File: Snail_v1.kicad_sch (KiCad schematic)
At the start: 2 parts, among them U1 PAM8406D, U2 STM32G431K6Tx

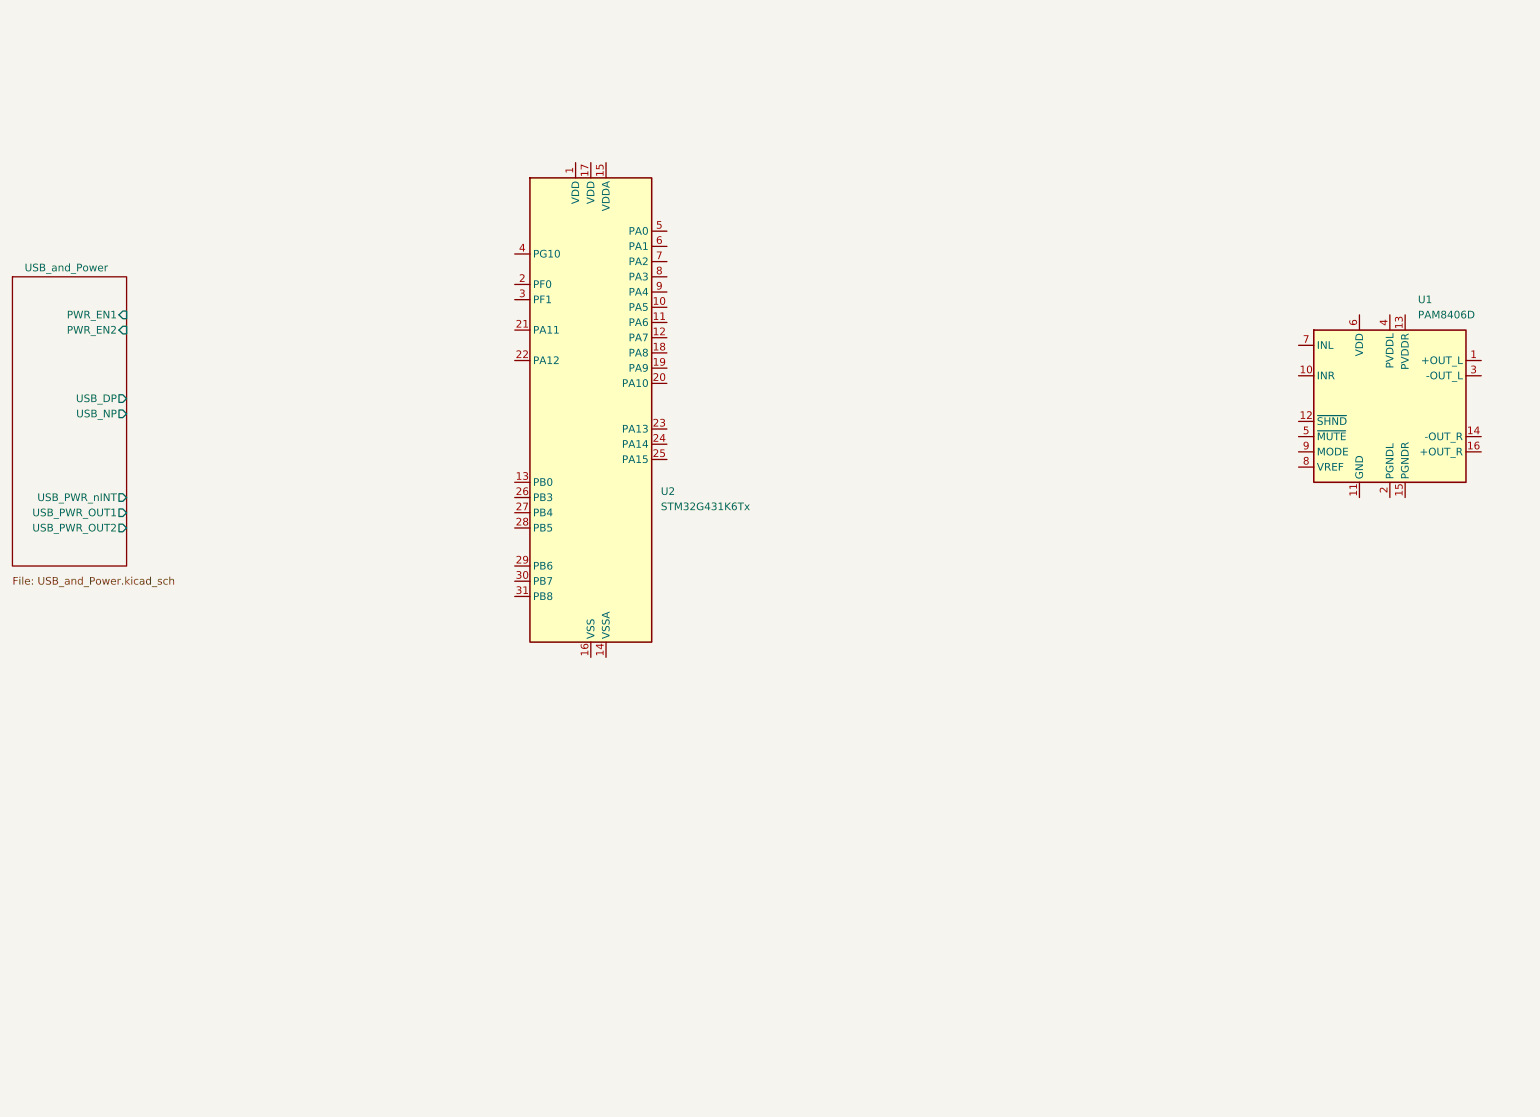
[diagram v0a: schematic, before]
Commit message: Added 5V, 3V3, PAM circuit
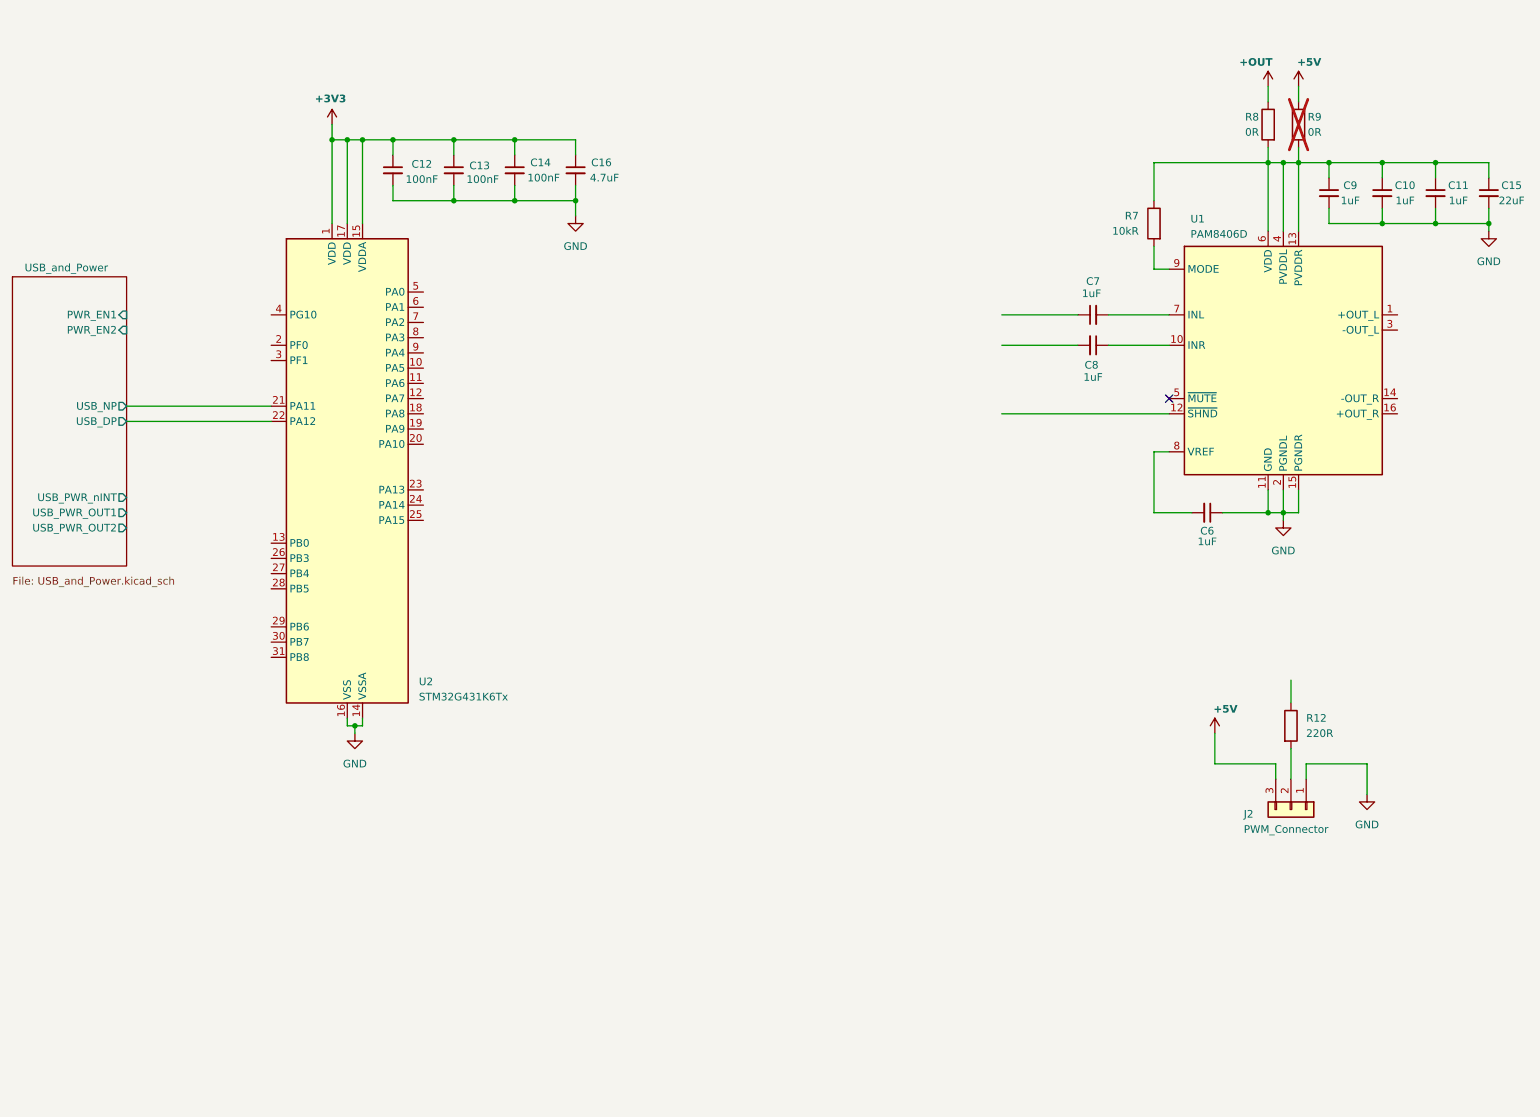
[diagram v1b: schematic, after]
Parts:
- added C10, C11, C6, C7, C8, C9: 1uF, symbol Device:C_Small
- added C12, C13, C14: 100nF, symbol Device:C_Small
- added C15: 22uF, symbol Device:C_Small
- added C16: 4.7uF, symbol Device:C_Small
- added J2: PWM_Connector, symbol Connector_Generic:Conn_01x03
- added R12: 220R, symbol Device:R
- added R7: 10kR, symbol Device:R
- added R8, R9: 0R, symbol Device:R
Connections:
- net USB_and_Power/USB_DP: now also U2.22 (PA12)
- net USB_and_Power/USB_NP: now also U2.21 (PA11)
- net at U1.10 (INR): now also C8.1
- net GND: now reaches U1.11 (GND)
- net GND: now also U1.15 (PGNDR), U1.2 (PGNDL), U2.14 (VSSA), U2.16 (VSS), U2.32 (VSS), C10.2, C11.2, C12.2, C13.2, C14.2, C15.2, C16.2, C6.1, C9.2, J2.1 (Pin_1)
- net at U1.13 (PVDDR): now also U1.4 (PVDDL), U1.6 (VDD), C10.1, C11.1, C15.1, C9.1, R7.1, R8.2, R9.2
- net at U1.7 (INL): now also C7.2
- net at U1.8 (VREF): now also C6.2
- net at U1.9 (MODE): now also R7.2
- net +3V3: now reaches U2.1 (VDD)
- net +3V3: now also U2.15 (VDDA), U2.17 (VDD), C12.1, C13.1, C14.1, C16.1
- new net: J2.2 (Pin_2), R12.2
- new net +5V: J2.3 (Pin_3), R9.1
- new net +OUT: R8.1
- no-connect marks 0 -> 1
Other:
- company: (none) -> Author: Christian R
- title: (none) -> Snail v1
- moved on the sheet: U1, U2

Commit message: Added BY25Q32 extFlash
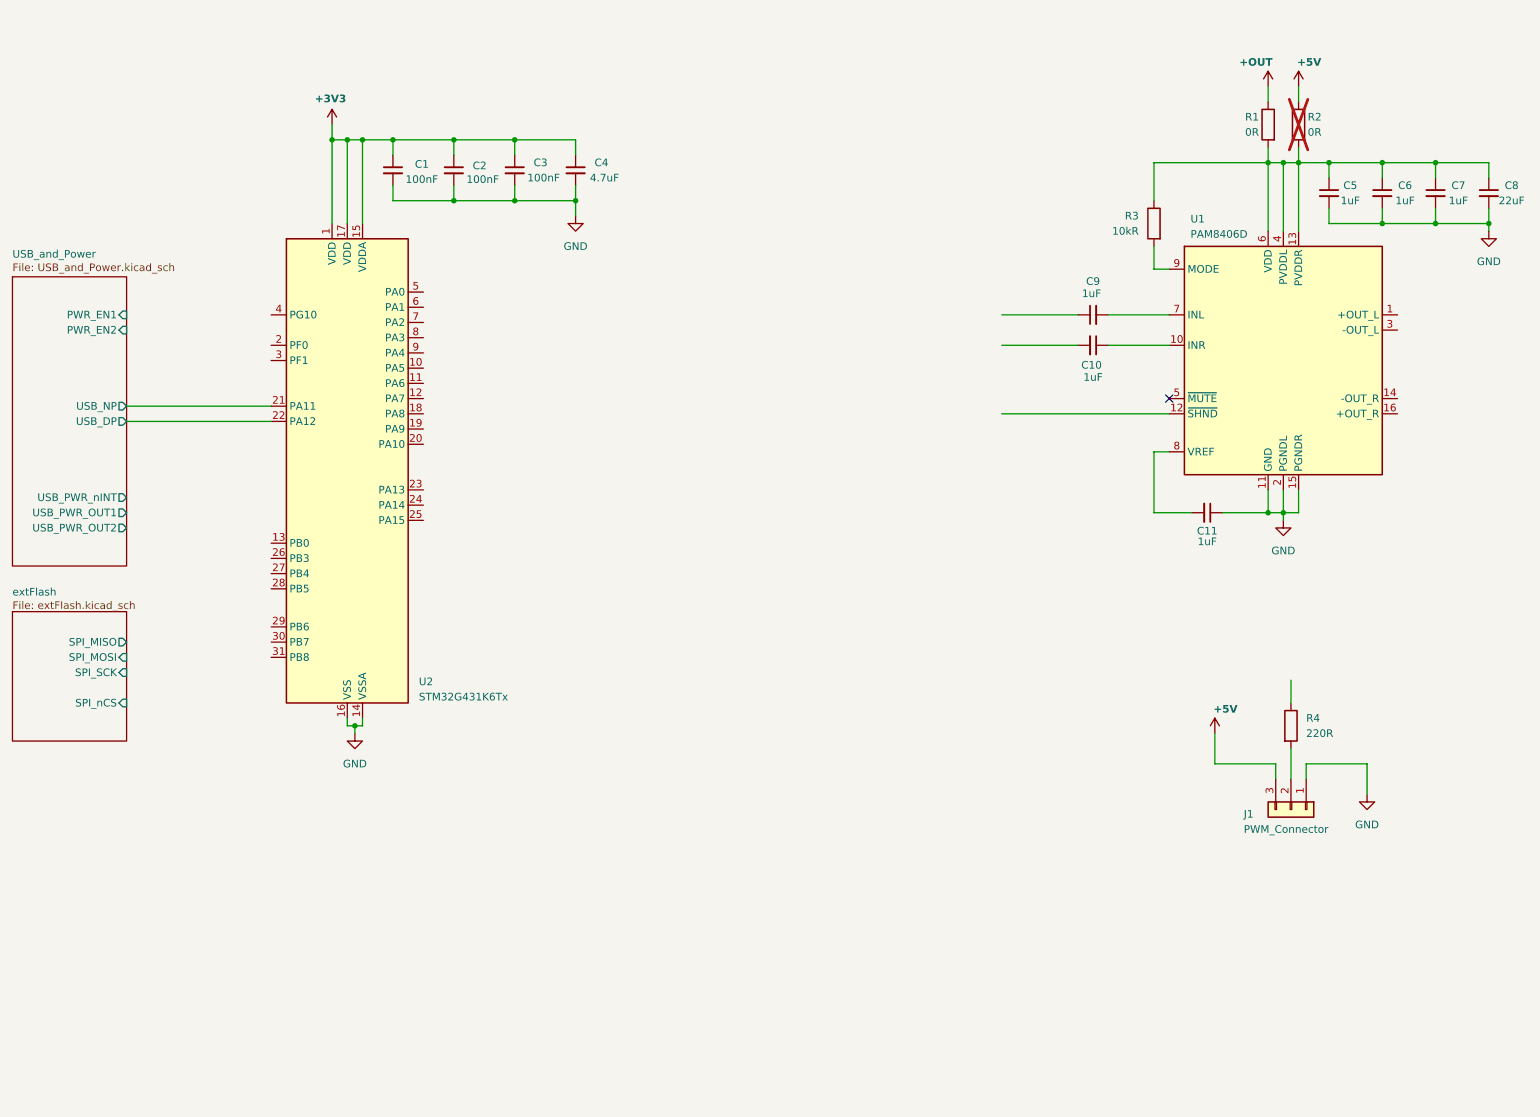
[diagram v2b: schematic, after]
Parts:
- renumbered C12 to C1, C8 to C10, C6 to C11, C13 to C2, C14 to C3, C16 to C4, C9 to C5, C10 to C6, C11 to C7, C15 to C8, C7 to C9, J2 to J1, R8 to R1, R9 to R2, R7 to R3, R12 to R4
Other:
- added sheet extFlash (extFlash.kicad_sch)
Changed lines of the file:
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@@
 		(on_board yes)
 		(dnp no)
-		(property "Reference" "#PWR023"
+		(property "Reference" "#PWR03"
 			(at 80.01 34.29 0)
 			(effects
@@
 			(project ""
 				(path "/98695d9f-8521-4f7d-bb41-f22c1215a8e7"
-					(reference "#PWR023")
+					(reference "#PWR03")
 					(unit 1)
 				)
@@
 		(dnp no)
 		(fields_autoplaced yes)
-		(property "Reference" "R12"
+		(property "Reference" "R4"
 			(at 242.57 129.5399 0)
 			(effects
@@
 			(project ""
 				(path "/98695d9f-8521-4f7d-bb41-f22c1215a8e7"
-					(reference "R12")
+					(reference "R4")
 					(unit 1)
 				)
@@
 		(on_board yes)
 		(dnp no)
-		(property "Reference" "C6"
+		(property "Reference" "C11"
 			(at 226.06 98.298 90)
 			(effects
@@
 			(project ""
 				(path "/98695d9f-8521-4f7d-bb41-f22c1215a8e7"
-					(reference "C6")
+					(reference "C11")
 					(unit 1)
 				)
@@
 		(dnp no)
 		(fields_autoplaced yes)
-		(property "Reference" "#PWR014"
+		(property "Reference" "#PWR06"
 			(at 238.76 102.87 0)
 			(effects
@@
 			(project ""
 				(path "/98695d9f-8521-4f7d-bb41-f22c1215a8e7"
-					(reference "#PWR014")
+					(reference "#PWR06")
 					(unit 1)
 				)
@@
 		(on_board yes)
 		(dnp no)
-		(property "Reference" "#PWR025"
+		(property "Reference" "#PWR08"
 			(at 227.33 135.89 0)
 			(effects
@@
 			(project "Snail_v1"
 				(path "/98695d9f-8521-4f7d-bb41-f22c1215a8e7"
-					(reference "#PWR025")
+					(reference "#PWR08")
 					(unit 1)
 				)
@@
 		(on_board yes)
 		(dnp no)
-		(property "Reference" "C16"
+		(property "Reference" "C4"
 			(at 124.968 36.83 0)
 			(effects
@@
 			(project "Snail_v1"
 				(path "/98695d9f-8521-4f7d-bb41-f22c1215a8e7"
-					(reference "C16")
+					(reference "C4")
 					(unit 1)
 				)
@@
 		(dnp no)
 		(fields_autoplaced yes)
-		(property "Reference" "#PWR013"
+		(property "Reference" "#PWR07"
 			(at 83.82 138.43 0)
 			(effects
@@
 			(project ""
 				(path "/98695d9f-8521-4f7d-bb41-f22c1215a8e7"
-					(reference "#PWR013")
+					(reference "#PWR07")
 					(unit 1)
 				)
@@
 		(on_board yes)
 		(dnp no)
-		(property "Reference" "R7"
+		(property "Reference" "R3"
 			(at 214.63 45.7199 0)
 			(effects
@@
 			(project ""
 				(path "/98695d9f-8521-4f7d-bb41-f22c1215a8e7"
-					(reference "R7")
+					(reference "R3")
 					(unit 1)
 				)
@@
 		(on_board yes)
 		(dnp no)
-		(property "Reference" "C9"
+		(property "Reference" "C5"
 			(at 249.936 40.64 0)
 			(effects
@@
 			(project "Snail_v1"
 				(path "/98695d9f-8521-4f7d-bb41-f22c1215a8e7"
-					(reference "C9")
+					(reference "C5")
 					(unit 1)
 				)
@@
 		(on_board yes)
 		(dnp no)
-		(property "Reference" "C15"
+		(property "Reference" "C8"
 			(at 276.86 40.64 0)
 			(effects
@@
 			(project "Snail_v1"
 				(path "/98695d9f-8521-4f7d-bb41-f22c1215a8e7"
-					(reference "C15")
+					(reference "C8")
 					(unit 1)
 				)
@@
 		(dnp no)
 		(fields_autoplaced yes)
-		(property "Reference" "#PWR015"
+		(property "Reference" "#PWR05"
 			(at 273.05 54.61 0)
 			(effects
@@
 			(project "Snail_v1"
 				(path "/98695d9f-8521-4f7d-bb41-f22c1215a8e7"
-					(reference "#PWR015")
+					(reference "#PWR05")
 					(unit 1)
 				)
@@
 		(on_board yes)
 		(dnp no)
-		(property "Reference" "C14"
+		(property "Reference" "C3"
 			(at 114.808 36.83 0)
 			(effects
@@
 			(project "Snail_v1"
 				(path "/98695d9f-8521-4f7d-bb41-f22c1215a8e7"
-					(reference "C14")
+					(reference "C3")
 					(unit 1)
 				)
@@
 		(on_board yes)
 		(dnp no)
-		(property "Reference" "C10"
+		(property "Reference" "C6"
 			(at 259.08 40.64 0)
 			(effects
@@
 			(project "Snail_v1"
 				(path "/98695d9f-8521-4f7d-bb41-f22c1215a8e7"
-					(reference "C10")
+					(reference "C6")
 					(unit 1)
 				)
@@
 		(on_board yes)
 		(dnp no)
-		(property "Reference" "#PWR018"
+		(property "Reference" "#PWR02"
 			(at 241.3 27.94 0)
 			(effects
@@
 			(project ""
 				(path "/98695d9f-8521-4f7d-bb41-f22c1215a8e7"
-					(reference "#PWR018")
+					(reference "#PWR02")
 					(unit 1)
 				)
@@
 		(on_board yes)
 		(dnp no)
-		(property "Reference" "C8"
+		(property "Reference" "C10"
 			(at 206.756 70.612 90)
 			(effects
@@
 			(project "Snail_v1"
 				(path "/98695d9f-8521-4f7d-bb41-f22c1215a8e7"
-					(reference "C8")
+					(reference "C10")
 					(unit 1)
 				)
@@
 		(on_board yes)
 		(dnp no)
-		(property "Reference" "C13"
+		(property "Reference" "C2"
 			(at 104.6416 37.338 0)
 			(effects
@@
 			(project "Snail_v1"
 				(path "/98695d9f-8521-4f7d-bb41-f22c1215a8e7"
-					(reference "C13")
+					(reference "C2")
 					(unit 1)
 				)
@@
 		(on_board yes)
 		(dnp no)
-		(property "Reference" "C11"
+		(property "Reference" "C7"
 			(at 267.97 40.64 0)
 			(effects
@@
 			(project "Snail_v1"
 				(path "/98695d9f-8521-4f7d-bb41-f22c1215a8e7"
-					(reference "C11")
+					(reference "C7")
 					(unit 1)
 				)
@@
 		(dnp no)
 		(fields_autoplaced yes)
-		(property "Reference" "#PWR016"
+		(property "Reference" "#PWR04"
 			(at 120.65 52.07 0)
 			(effects
@@
 			(project "Snail_v1"
 				(path "/98695d9f-8521-4f7d-bb41-f22c1215a8e7"
-					(reference "#PWR016")
+					(reference "#PWR04")
 					(unit 1)
 				)
@@
 		(on_board yes)
 		(dnp no)
-		(property "Reference" "R8"
+		(property "Reference" "R1"
 			(at 234.696 29.21 0)
 			(effects
@@
 			(project "Snail_v1"
 				(path "/98695d9f-8521-4f7d-bb41-f22c1215a8e7"
-					(reference "R8")
+					(reference "R1")
 					(unit 1)
 				)
@@
 		(dnp no)
 		(fields_autoplaced yes)
-		(property "Reference" "#PWR024"
+		(property "Reference" "#PWR09"
 			(at 252.73 148.59 0)
 			(effects
@@
 			(project "Snail_v1"
 				(path "/98695d9f-8521-4f7d-bb41-f22c1215a8e7"
-					(reference "#PWR024")
+					(reference "#PWR09")
 					(unit 1)
 				)
@@
 		(on_board yes)
 		(dnp yes)
-		(property "Reference" "R9"
+		(property "Reference" "R2"
 			(at 242.824 29.21 0)
 			(effects
@@
 			(project "Snail_v1"
 				(path "/98695d9f-8521-4f7d-bb41-f22c1215a8e7"
-					(reference "R9")
+					(reference "R2")
 					(unit 1)
 				)
@@
 		(on_board yes)
 		(dnp no)
-		(property "Reference" "#PWR017"
+		(property "Reference" "#PWR01"
 			(at 236.22 27.94 0)
 			(effects
@@
 			(project "Snail_v1"
 				(path "/98695d9f-8521-4f7d-bb41-f22c1215a8e7"
-					(reference "#PWR017")
+					(reference "#PWR01")
 					(unit 1)
 				)
@@
 		(on_board yes)
 		(dnp no)
-		(property "Reference" "C12"
+		(property "Reference" "C1"
 			(at 94.996 37.084 0)
 			(effects
@@
 			(project "Snail_v1"
 				(path "/98695d9f-8521-4f7d-bb41-f22c1215a8e7"
-					(reference "C12")
+					(reference "C1")
 					(unit 1)
 				)
@@
 		(on_board yes)
 		(dnp no)
-		(property "Reference" "J2"
+		(property "Reference" "J1"
 			(at 232.156 145.542 90)
 			(effects
@@
 			(project ""
 				(path "/98695d9f-8521-4f7d-bb41-f22c1215a8e7"
-					(reference "J2")
+					(reference "J1")
 					(unit 1)
 				)
@@
 		(on_board yes)
 		(dnp no)
-		(property "Reference" "C7"
+		(property "Reference" "C9"
 			(at 207.01 56.642 90)
 			(effects
@@
 			(project "Snail_v1"
 				(path "/98695d9f-8521-4f7d-bb41-f22c1215a8e7"
-					(reference "C7")
-					(unit 1)
+					(reference "C9")
+					(unit 1)
+				)
+			)
+		)
+	)
+	(sheet
+		(at 26.67 111.76)
+		(size 19.05 21.59)
+		(exclude_from_sim no)
+		(in_bom yes)
+		(on_board yes)
+		(dnp no)
+		(stroke
+			(width 0.1524)
+			(type solid)
+		)
+		(fill
+			(color 0 0 0 0.0000)
+		)
+		(property "Sheetname" "extFlash"
+			(at 26.67 109.22 0)
+			(effects
+				(font
+					(size 1.27 1.27)
+				)
+				(justify left bottom)
+			)
+		)
+		(property "Sheetfile" "extFlash.kicad_sch"
+			(at 26.67 109.982 0)
+			(effects
+				(font
+					(size 1.27 1.27)
+				)
+				(justify left top)
+			)
+		)
+		(pin "SPI_MISO" output
+			(at 45.72 116.84 0)
+			(effects
+				(font
+					(size 1.27 1.27)
+				)
+				(justify right)
+			)
+		)
+		(pin "SPI_MOSI" input
+			(at 45.72 119.38 0)
+			(effects
+				(font
+					(size 1.27 1.27)
+				)
+				(justify right)
+			)
+		)
+		(pin "SPI_nCS" input
+			(at 45.72 127 0)
+			(effects
+				(font
+					(size 1.27 1.27)
+				)
+				(justify right)
+			)
+		)
+		(pin "SPI_SCK" input
+			(at 45.72 121.92 0)
+			(effects
+				(font
+					(size 1.27 1.27)
+				)
+				(justify right)
+			)
+		)
+		(instances
+			(project "Snail_v1"
+				(path "/98695d9f-8521-4f7d-bb41-f22c1215a8e7"
+					(page "3")
 				)
 			)
@@
 		)
 		(property "Sheetname" "USB_and_Power"
-			(at 28.702 55.118 0)
+			(at 26.67 52.832 0)
 			(effects
 				(font
@@
 		)
 		(property "Sheetfile" "USB_and_Power.kicad_sch"
-			(at 26.67 105.918 0)
-			(effects
-				(font
+			(at 26.67 53.594 0)
+			(effects
+				(font
